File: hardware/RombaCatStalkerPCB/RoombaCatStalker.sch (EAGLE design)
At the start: 3 parts, among them IC1 DLP-USB232M-G, J1 POWER_JACKPTH

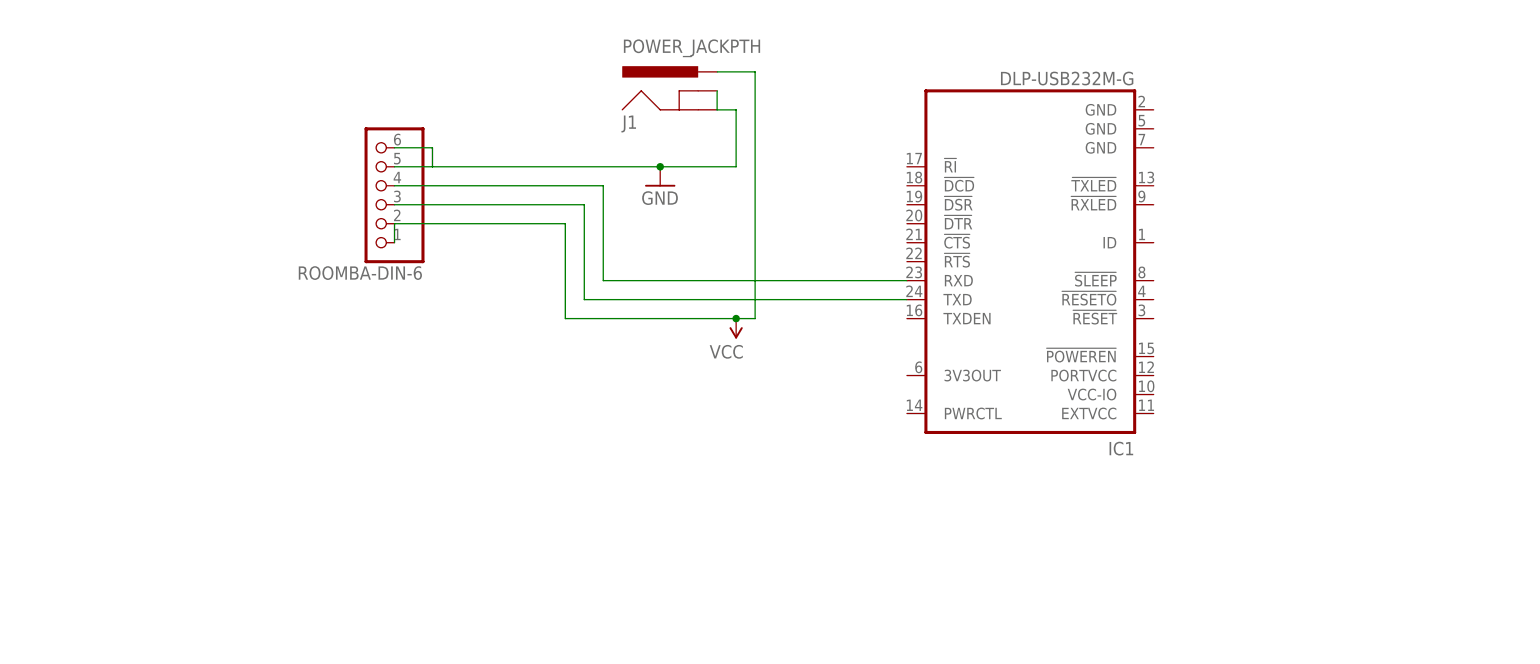
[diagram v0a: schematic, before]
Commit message: Schematic change, forgot about the DC/DC Converter
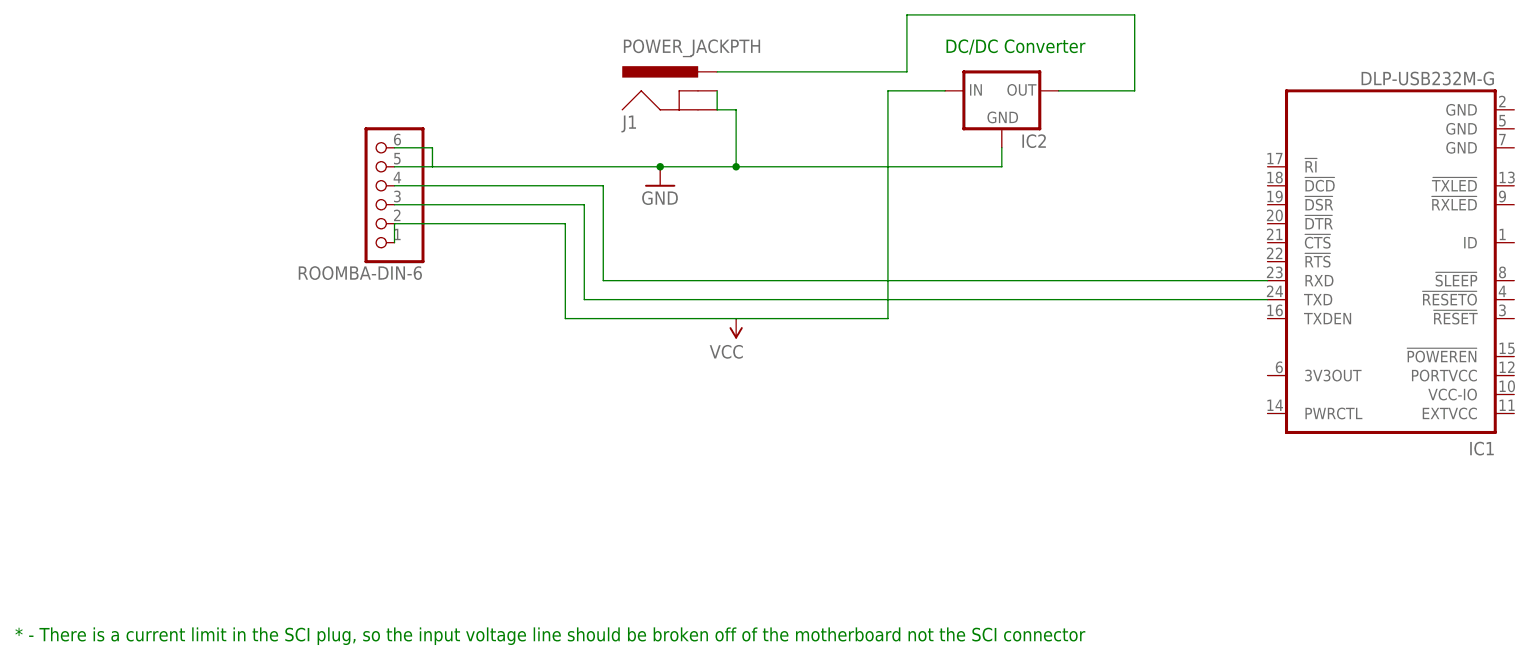
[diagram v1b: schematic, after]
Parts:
- added IC2: (no value), v-reg:XC63FPL
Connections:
- new net N$6: IC2.OUT, J1.PWR
- net GND: now also IC2.GND
- net VCC: now also IC2.IN; no longer J1.PWR
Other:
- note added: "* - There is a current limit in the SCI plug, so the input voltage line should be broken off of the motherboard not the SCI connector"
- note added: "DC/DC Converter"
- moved on the sheet: IC1
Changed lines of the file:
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@@
 <part name="P+1" library="spk1" deviceset="VCC" device=""/>
 <part name="J1" library="spk1" deviceset="POWER_JACK" device="PTH"/>
+<part name="IC2" library="v-reg" deviceset="XC63FP" device="L"/>
 </parts>
 <sheets>
@@
 <plain>
 <text x="30.48" y="139.7" size="1.778" layer="150">Roomba DIN 6 Connector</text>
-<text x="116.84" y="147.32" size="1.778" layer="150">FTDI Serial to USB Chip</text>
+<text x="165.1" y="147.32" size="1.778" layer="150">FTDI Serial to USB Chip</text>
+<text x="116.84" y="147.32" size="1.778" layer="91">DC/DC Converter</text>
+<text x="-7.62" y="68.58" size="1.778" layer="91">* - There is a current limit in the SCI plug, so the input voltage line should be broken off of the motherboard not the SCI connector</text>
 </plain>
 <instances>
 <instance part="ROOMBA-DIN-6" gate="A" x="40.64" y="129.54" rot="R180"/>
-<instance part="IC1" gate="GND@1" x="129.54" y="119.38" rot="R180"/>
+<instance part="IC1" gate="GND@1" x="177.8" y="119.38" rot="R180"/>
 <instance part="FRAME1" gate="G$1" x="-22.86" y="40.64"/>
 <instance part="GND1" gate="1" x="78.74" y="129.54"/>
 <instance part="P+1" gate="1" x="88.9" y="111.76" rot="R180"/>
 <instance part="J1" gate="G$1" x="83.82" y="137.16"/>
+<instance part="IC2" gate="G$1" x="124.46" y="142.24"/>
 </instances>
 <busses>
@@
 <wire x1="68.58" y1="127" x2="68.58" y2="114.3" width="0.1524" layer="91"/>
 <pinref part="IC1" gate="GND@1" pin="TXD"/>
-<wire x1="68.58" y1="114.3" x2="111.76" y2="114.3" width="0.1524" layer="91"/>
+<wire x1="68.58" y1="114.3" x2="160.02" y2="114.3" width="0.1524" layer="91"/>
 </segment>
 </net>
@@
 <wire x1="71.12" y1="129.54" x2="71.12" y2="116.84" width="0.1524" layer="91"/>
 <pinref part="IC1" gate="GND@1" pin="RXD"/>
-<wire x1="71.12" y1="116.84" x2="111.76" y2="116.84" width="0.1524" layer="91"/>
+<wire x1="71.12" y1="116.84" x2="160.02" y2="116.84" width="0.1524" layer="91"/>
 </segment>
 </net>
@@
 <pinref part="GND1" gate="1" pin="GND"/>
 <junction x="78.74" y="132.08"/>
+<pinref part="IC2" gate="G$1" pin="GND"/>
+<wire x1="124.46" y1="134.62" x2="124.46" y2="132.08" width="0.1524" layer="91"/>
+<wire x1="124.46" y1="132.08" x2="88.9" y2="132.08" width="0.1524" layer="91"/>
+<junction x="88.9" y="132.08"/>
 </segment>
 </net>
 <net name="VCC" class="0">
 <segment>
-<pinref part="J1" gate="G$1" pin="PWR"/>
-<wire x1="86.36" y1="144.78" x2="91.44" y2="144.78" width="0.1524" layer="91"/>
-<wire x1="91.44" y1="144.78" x2="91.44" y2="111.76" width="0.1524" layer="91"/>
-<wire x1="91.44" y1="111.76" x2="88.9" y2="111.76" width="0.1524" layer="91"/>
 <wire x1="88.9" y1="111.76" x2="66.04" y2="111.76" width="0.1524" layer="91"/>
 <wire x1="66.04" y1="111.76" x2="66.04" y2="124.46" width="0.1524" layer="91"/>
@@
 <wire x1="43.18" y1="124.46" x2="43.18" y2="121.92" width="0.1524" layer="91"/>
 <pinref part="P+1" gate="1" pin="VCC"/>
-<junction x="88.9" y="111.76"/>
+<pinref part="IC2" gate="G$1" pin="IN"/>
+<wire x1="116.84" y1="142.24" x2="109.22" y2="142.24" width="0.1524" layer="91"/>
+<wire x1="109.22" y1="142.24" x2="109.22" y2="111.76" width="0.1524" layer="91"/>
+<wire x1="109.22" y1="111.76" x2="88.9" y2="111.76" width="0.1524" layer="91"/>
 </segment>
 </net>
+<net name="N$6" class="0">
+<segment>
+<pinref part="IC2" gate="G$1" pin="OUT"/>
+<pinref part="J1" gate="G$1" pin="PWR"/>
+<wire x1="86.36" y1="144.78" x2="111.76" y2="144.78" width="0.1524" layer="91"/>
+<wire x1="111.76" y1="144.78" x2="111.76" y2="152.4" width="0.1524" layer="91"/>
+<wire x1="111.76" y1="152.4" x2="142.24" y2="152.4" width="0.1524" layer="91"/>
+<wire x1="142.24" y1="152.4" x2="142.24" y2="142.24" width="0.1524" layer="91"/>
+<wire x1="142.24" y1="142.24" x2="132.08" y2="142.24" width="0.1524" layer="91"/>
+</segment>
+</net>
